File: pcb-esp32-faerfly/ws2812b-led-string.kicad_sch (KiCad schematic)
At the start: 24 parts

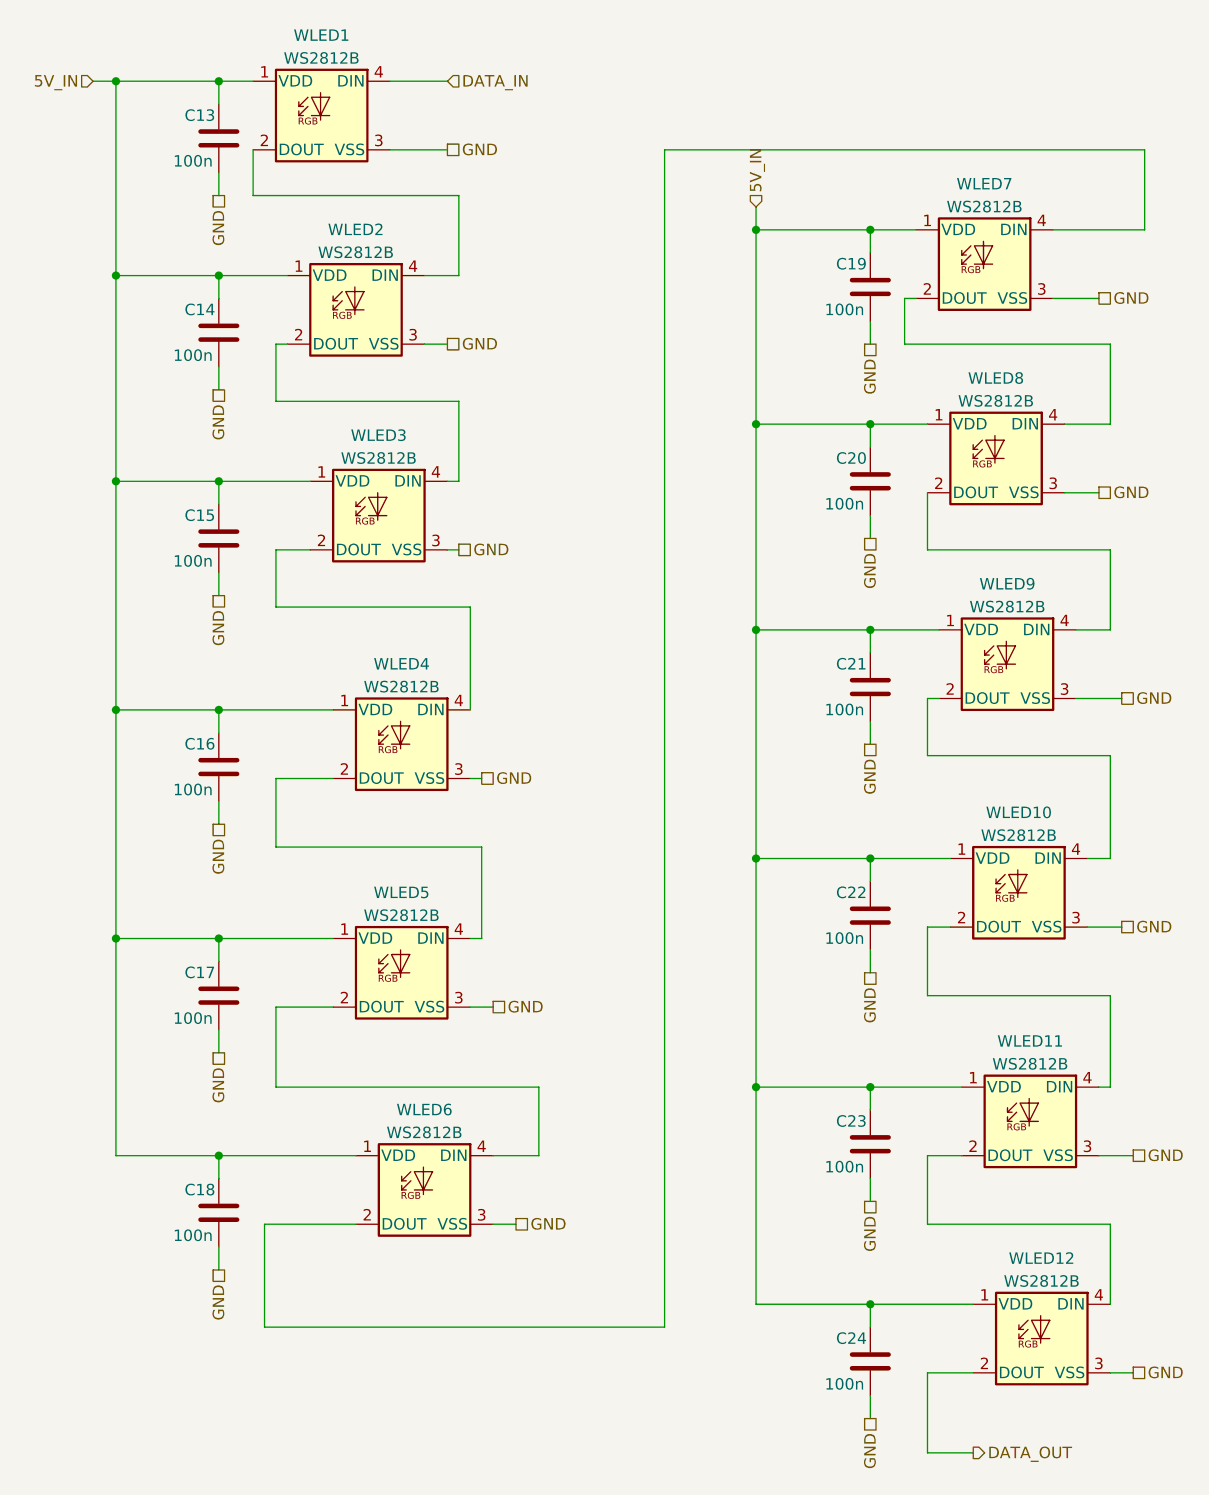
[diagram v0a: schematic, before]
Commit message: Added Complete BOM
Ready for Parts Shopping!
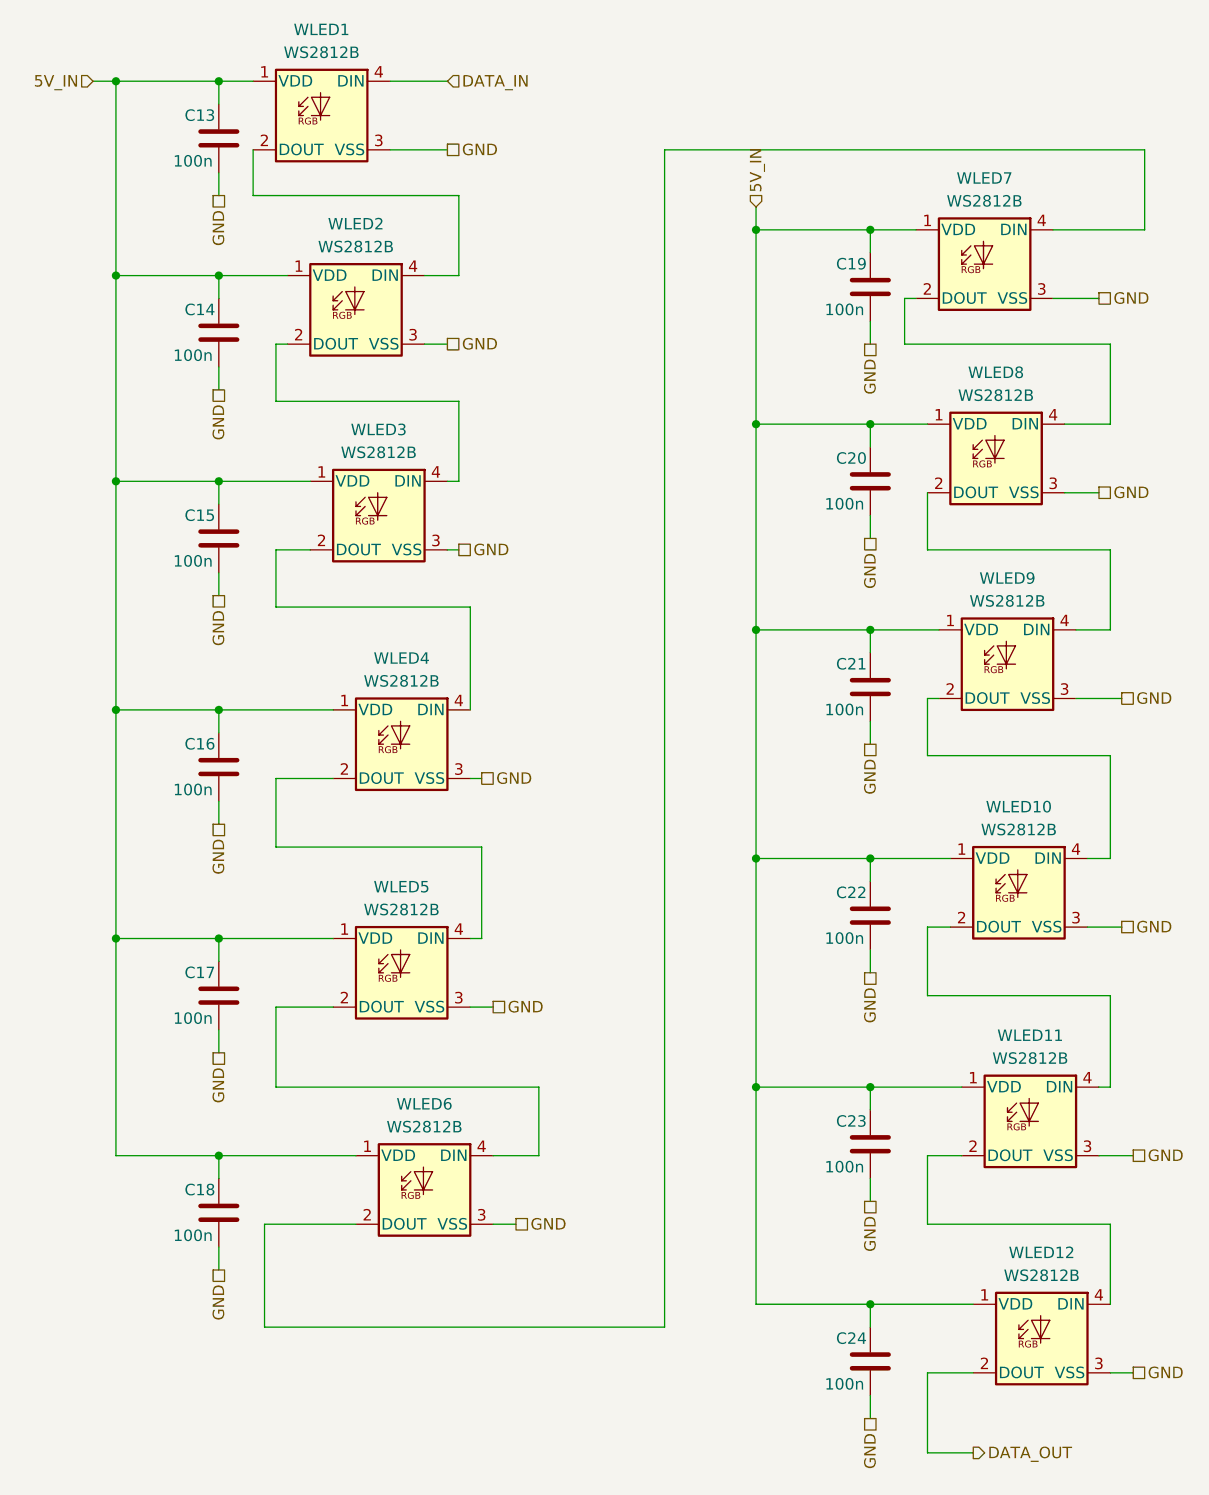
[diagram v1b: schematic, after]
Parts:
- WLED1, WLED10, WLED11, WLED12, WLED2, WLED3, WLED4, WLED5, WLED6, WLED7, WLED8, WLED9: Cost (none) -> 0.0768; JLCpart (none) -> C2920042
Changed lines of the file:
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@@
   (symbol (lib_id "000_Diodes_Immo:WS2812B") (at 67.945 55.245 0) (unit 1)
     (in_bom yes) (on_board yes) (dnp no) (fields_autoplaced)
-    (property "Reference" "WLED2" (at 67.945 46.355 0)
-      (effects (font (size 1.27 1.27)))
-    )
-    (property "Value" "WS2812B" (at 67.945 48.895 0)
+    (property "Reference" "WLED2" (at 67.945 45.72 0)
+      (effects (font (size 1.27 1.27)))
+    )
+    (property "Value" "WS2812B" (at 67.945 48.26 0)
       (effects (font (size 1.27 1.27)))
     )
@@
       (effects (font (size 1.27 1.27)) (justify left top) hide)
     )
+    (property "JLCpart" "C2920042" (at 67.945 55.245 0)
+      (effects (font (size 1.27 1.27)) hide)
+    )
+    (property "Cost" "0.0768" (at 67.945 55.245 0)
+      (effects (font (size 1.27 1.27)) hide)
+    )
     (pin "1")
     (pin "2")
@@
   (symbol (lib_id "000_Diodes_Immo:WS2812B") (at 70.485 78.105 0) (unit 1)
     (in_bom yes) (on_board yes) (dnp no) (fields_autoplaced)
-    (property "Reference" "WLED3" (at 70.485 69.215 0)
-      (effects (font (size 1.27 1.27)))
-    )
-    (property "Value" "WS2812B" (at 70.485 71.755 0)
+    (property "Reference" "WLED3" (at 70.485 68.58 0)
+      (effects (font (size 1.27 1.27)))
+    )
+    (property "Value" "WS2812B" (at 70.485 71.12 0)
       (effects (font (size 1.27 1.27)))
     )
@@
       (effects (font (size 1.27 1.27)) (justify left top) hide)
     )
+    (property "JLCpart" "C2920042" (at 70.485 78.105 0)
+      (effects (font (size 1.27 1.27)) hide)
+    )
+    (property "Cost" "0.0768" (at 70.485 78.105 0)
+      (effects (font (size 1.27 1.27)) hide)
+    )
     (pin "1")
     (pin "2")
@@
   (symbol (lib_id "000_Diodes_Immo:WS2812B") (at 137.795 50.165 0) (unit 1)
     (in_bom yes) (on_board yes) (dnp no) (fields_autoplaced)
-    (property "Reference" "WLED7" (at 137.795 41.275 0)
-      (effects (font (size 1.27 1.27)))
-    )
-    (property "Value" "WS2812B" (at 137.795 43.815 0)
+    (property "Reference" "WLED7" (at 137.795 40.64 0)
+      (effects (font (size 1.27 1.27)))
+    )
+    (property "Value" "WS2812B" (at 137.795 43.18 0)
       (effects (font (size 1.27 1.27)))
     )
@@
       (effects (font (size 1.27 1.27)) (justify left top) hide)
     )
+    (property "JLCpart" "C2920042" (at 137.795 50.165 0)
+      (effects (font (size 1.27 1.27)) hide)
+    )
+    (property "Cost" "0.0768" (at 137.795 50.165 0)
+      (effects (font (size 1.27 1.27)) hide)
+    )
     (pin "1")
     (pin "2")
@@
   (symbol (lib_id "000_Diodes_Immo:WS2812B") (at 144.145 169.545 0) (unit 1)
     (in_bom yes) (on_board yes) (dnp no) (fields_autoplaced)
-    (property "Reference" "WLED12" (at 144.145 160.655 0)
-      (effects (font (size 1.27 1.27)))
-    )
-    (property "Value" "WS2812B" (at 144.145 163.195 0)
+    (property "Reference" "WLED12" (at 144.145 160.02 0)
+      (effects (font (size 1.27 1.27)))
+    )
+    (property "Value" "WS2812B" (at 144.145 162.56 0)
       (effects (font (size 1.27 1.27)))
     )
@@
       (effects (font (size 1.27 1.27)) (justify left top) hide)
     )
+    (property "JLCpart" "C2920042" (at 144.145 169.545 0)
+      (effects (font (size 1.27 1.27)) hide)
+    )
+    (property "Cost" "0.0768" (at 144.145 169.545 0)
+      (effects (font (size 1.27 1.27)) hide)
+    )
     (pin "1")
     (pin "2")
@@
   (symbol (lib_id "000_Diodes_Immo:WS2812B") (at 75.565 153.035 0) (unit 1)
     (in_bom yes) (on_board yes) (dnp no) (fields_autoplaced)
-    (property "Reference" "WLED6" (at 75.565 144.145 0)
-      (effects (font (size 1.27 1.27)))
-    )
-    (property "Value" "WS2812B" (at 75.565 146.685 0)
+    (property "Reference" "WLED6" (at 75.565 143.51 0)
+      (effects (font (size 1.27 1.27)))
+    )
+    (property "Value" "WS2812B" (at 75.565 146.05 0)
       (effects (font (size 1.27 1.27)))
     )
@@
       (effects (font (size 1.27 1.27)) (justify left top) hide)
     )
+    (property "JLCpart" "C2920042" (at 75.565 153.035 0)
+      (effects (font (size 1.27 1.27)) hide)
+    )
+    (property "Cost" "0.0768" (at 75.565 153.035 0)
+      (effects (font (size 1.27 1.27)) hide)
+    )
     (pin "1")
     (pin "2")
@@
   (symbol (lib_id "000_Diodes_Immo:WS2812B") (at 73.025 103.505 0) (unit 1)
     (in_bom yes) (on_board yes) (dnp no) (fields_autoplaced)
-    (property "Reference" "WLED4" (at 73.025 94.615 0)
-      (effects (font (size 1.27 1.27)))
-    )
-    (property "Value" "WS2812B" (at 73.025 97.155 0)
+    (property "Reference" "WLED4" (at 73.025 93.98 0)
+      (effects (font (size 1.27 1.27)))
+    )
+    (property "Value" "WS2812B" (at 73.025 96.52 0)
       (effects (font (size 1.27 1.27)))
     )
@@
       (effects (font (size 1.27 1.27)) (justify left top) hide)
     )
+    (property "JLCpart" "C2920042" (at 73.025 103.505 0)
+      (effects (font (size 1.27 1.27)) hide)
+    )
+    (property "Cost" "0.0768" (at 73.025 103.505 0)
+      (effects (font (size 1.27 1.27)) hide)
+    )
     (pin "1")
     (pin "2")
@@
   (symbol (lib_id "000_Diodes_Immo:WS2812B") (at 64.135 33.655 0) (unit 1)
     (in_bom yes) (on_board yes) (dnp no) (fields_autoplaced)
-    (property "Reference" "WLED1" (at 64.135 24.765 0)
-      (effects (font (size 1.27 1.27)))
-    )
-    (property "Value" "WS2812B" (at 64.135 27.305 0)
+    (property "Reference" "WLED1" (at 64.135 24.13 0)
+      (effects (font (size 1.27 1.27)))
+    )
+    (property "Value" "WS2812B" (at 64.135 26.67 0)
       (effects (font (size 1.27 1.27)))
     )
@@
       (effects (font (size 1.27 1.27)) (justify left top) hide)
     )
+    (property "JLCpart" "C2920042" (at 64.135 33.655 0)
+      (effects (font (size 1.27 1.27)) hide)
+    )
+    (property "Cost" "0.0768" (at 64.135 33.655 0)
+      (effects (font (size 1.27 1.27)) hide)
+    )
     (pin "1")
     (pin "2")
@@
   (symbol (lib_id "000_Diodes_Immo:WS2812B") (at 140.335 94.615 0) (unit 1)
     (in_bom yes) (on_board yes) (dnp no) (fields_autoplaced)
-    (property "Reference" "WLED9" (at 140.335 85.725 0)
-      (effects (font (size 1.27 1.27)))
-    )
-    (property "Value" "WS2812B" (at 140.335 88.265 0)
+    (property "Reference" "WLED9" (at 140.335 85.09 0)
+      (effects (font (size 1.27 1.27)))
+    )
+    (property "Value" "WS2812B" (at 140.335 87.63 0)
       (effects (font (size 1.27 1.27)))
     )
@@
       (effects (font (size 1.27 1.27)) (justify left top) hide)
     )
+    (property "JLCpart" "C2920042" (at 140.335 94.615 0)
+      (effects (font (size 1.27 1.27)) hide)
+    )
+    (property "Cost" "0.0768" (at 140.335 94.615 0)
+      (effects (font (size 1.27 1.27)) hide)
+    )
     (pin "1")
     (pin "2")
@@
   (symbol (lib_id "000_Diodes_Immo:WS2812B") (at 139.065 71.755 0) (unit 1)
     (in_bom yes) (on_board yes) (dnp no) (fields_autoplaced)
-    (property "Reference" "WLED8" (at 139.065 62.865 0)
-      (effects (font (size 1.27 1.27)))
-    )
-    (property "Value" "WS2812B" (at 139.065 65.405 0)
+    (property "Reference" "WLED8" (at 139.065 62.23 0)
+      (effects (font (size 1.27 1.27)))
+    )
+    (property "Value" "WS2812B" (at 139.065 64.77 0)
       (effects (font (size 1.27 1.27)))
     )
@@
       (effects (font (size 1.27 1.27)) (justify left top) hide)
     )
+    (property "JLCpart" "C2920042" (at 139.065 71.755 0)
+      (effects (font (size 1.27 1.27)) hide)
+    )
+    (property "Cost" "0.0768" (at 139.065 71.755 0)
+      (effects (font (size 1.27 1.27)) hide)
+    )
     (pin "1")
     (pin "2")
@@
   (symbol (lib_id "000_Diodes_Immo:WS2812B") (at 141.605 120.015 0) (unit 1)
     (in_bom yes) (on_board yes) (dnp no) (fields_autoplaced)
-    (property "Reference" "WLED10" (at 141.605 111.125 0)
-      (effects (font (size 1.27 1.27)))
-    )
-    (property "Value" "WS2812B" (at 141.605 113.665 0)
+    (property "Reference" "WLED10" (at 141.605 110.49 0)
+      (effects (font (size 1.27 1.27)))
+    )
+    (property "Value" "WS2812B" (at 141.605 113.03 0)
       (effects (font (size 1.27 1.27)))
     )
@@
       (effects (font (size 1.27 1.27)) (justify left top) hide)
     )
+    (property "JLCpart" "C2920042" (at 141.605 120.015 0)
+      (effects (font (size 1.27 1.27)) hide)
+    )
+    (property "Cost" "0.0768" (at 141.605 120.015 0)
+      (effects (font (size 1.27 1.27)) hide)
+    )
     (pin "1")
     (pin "2")
@@
   (symbol (lib_id "000_Diodes_Immo:WS2812B") (at 73.025 128.905 0) (unit 1)
     (in_bom yes) (on_board yes) (dnp no) (fields_autoplaced)
-    (property "Reference" "WLED5" (at 73.025 120.015 0)
-      (effects (font (size 1.27 1.27)))
-    )
-    (property "Value" "WS2812B" (at 73.025 122.555 0)
+    (property "Reference" "WLED5" (at 73.025 119.38 0)
+      (effects (font (size 1.27 1.27)))
+    )
+    (property "Value" "WS2812B" (at 73.025 121.92 0)
       (effects (font (size 1.27 1.27)))
     )
@@
       (effects (font (size 1.27 1.27)) (justify left top) hide)
     )
+    (property "JLCpart" "C2920042" (at 73.025 128.905 0)
+      (effects (font (size 1.27 1.27)) hide)
+    )
+    (property "Cost" "0.0768" (at 73.025 128.905 0)
+      (effects (font (size 1.27 1.27)) hide)
+    )
     (pin "1")
     (pin "2")
@@
   (symbol (lib_id "000_Diodes_Immo:WS2812B") (at 142.875 145.415 0) (unit 1)
     (in_bom yes) (on_board yes) (dnp no) (fields_autoplaced)
-    (property "Reference" "WLED11" (at 142.875 136.525 0)
-      (effects (font (size 1.27 1.27)))
-    )
-    (property "Value" "WS2812B" (at 142.875 139.065 0)
+    (property "Reference" "WLED11" (at 142.875 135.89 0)
+      (effects (font (size 1.27 1.27)))
+    )
+    (property "Value" "WS2812B" (at 142.875 138.43 0)
       (effects (font (size 1.27 1.27)))
     )
@@
       (effects (font (size 1.27 1.27)) (justify left top) hide)
     )
-    (pin "1")
+    (property "JLCpart" "C2920042" (at 142.875 145.415 0)
+      (effects (font (size 1.27 1.27)) hide)
+    )
+    (property "Cost" "0.0768" (at 142.875 145.415 0)
+      (effects (font (size 1.27 1.27)) hide)
+    )
+    (pin "1")
